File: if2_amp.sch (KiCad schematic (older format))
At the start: 23 parts, among them Q2 BC847BS, U3 MCP6D11

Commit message: Pcb vHA8KDA
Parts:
- added C?: 10n, Capacitor_SMD:C_0805_2012Metric_Pad1.18x1.45mm_HandSolder, symbol Device:C
- added R42, R43: 19k, Resistor_SMD:R_0805_2012Metric_Pad1.20x1.40mm_HandSolder, symbol Device:R
- C31, C32, C36, C37, C38: footprint Capacitor_SMD:C_0805_2012Metric_Pad1.15x1.40mm_HandSolder -> Capacitor_SMD:C_0805_2012Metric_Pad1.18x1.45mm_HandSolder
- R10, R13, R14, R15, R25, R9: footprint Resistor_SMD:R_0805_2012Metric_Pad1.15x1.40mm_HandSolder -> Resistor_SMD:R_0805_2012Metric_Pad1.20x1.40mm_HandSolder
- R12: footprint Resistor_SMD:R_1206_3216Metric_Pad1.42x1.75mm_HandSolder -> Resistor_SMD:R_0805_2012Metric_Pad1.20x1.40mm_HandSolder
- R35, R36, R37, R38, R39, R40, R41: footprint Resistor_SMD:R_1206_3216Metric_Pad1.42x1.75mm_HandSolder -> Resistor_SMD:R_1206_3216Metric_Pad1.30x1.75mm_HandSolder
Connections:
- net +5VA: now also R42.1
- net DC_CM: now also C32.1, R42.2, R43.1
- net GND: now also C32.2, R43.2
- net GNDA: now also C?.2; no longer C32.2
- net at Q2.2 (B1), Q2.5 (B2), R14.2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: now also C?.1; no longer C32.1
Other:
- moved on the sheet: C32
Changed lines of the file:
@@
 F 0 "R9" V 2193 2450 50  0000 C CNN
 F 1 "1.2k" V 2284 2450 50  0000 C CNN
-F 2 "Resistor_SMD:R_0805_2012Metric_Pad1.15x1.40mm_HandSolder" V 2330 2450 50  0001 C CNN
+F 2 "Resistor_SMD:R_0805_2012Metric_Pad1.20x1.40mm_HandSolder" V 2330 2450 50  0001 C CNN
 F 3 "~" H 2400 2450 50  0001 C CNN
 	1    2400 2450
@@
 F 0 "R10" V 2600 3850 50  0000 C CNN
 F 1 "1.2k" V 2500 3850 50  0000 C CNN
-F 2 "Resistor_SMD:R_0805_2012Metric_Pad1.15x1.40mm_HandSolder" V 2330 3850 50  0001 C CNN
+F 2 "Resistor_SMD:R_0805_2012Metric_Pad1.20x1.40mm_HandSolder" V 2330 3850 50  0001 C CNN
 F 3 "~" H 2400 3850 50  0001 C CNN
 	1    2400 3850
@@
 Wire Wire Line
 	3100 3250 3450 3250
-Wire Wire Line
-	2800 3150 2750 3150
 $Comp
 L power:+5VA #PWR0129
@@
 L Device:C C32
 U 1 1 5FEBE468
-P 7350 3500
-F 0 "C32" H 7465 3546 50  0000 L CNN
-F 1 "10n" H 7465 3455 50  0000 L CNN
-F 2 "Capacitor_SMD:C_0805_2012Metric_Pad1.15x1.40mm_HandSolder" H 7388 3350 50  0001 C CNN
-F 3 "~" H 7350 3500 50  0001 C CNN
-	1    7350 3500
+P 3850 4250
+F 0 "C32" H 3965 4296 50  0000 L CNN
+F 1 "10n" H 3965 4205 50  0000 L CNN
+F 2 "Capacitor_SMD:C_0805_2012Metric_Pad1.18x1.45mm_HandSolder" H 3888 4100 50  0001 C CNN
+F 3 "~" H 3850 4250 50  0001 C CNN
+	1    3850 4250
 	1    0    0    -1
 $EndComp
@@
 F 0 "R14" H 8670 3296 50  0000 L CNN
 F 1 "19k" H 8670 3205 50  0000 L CNN
-F 2 "Resistor_SMD:R_0805_2012Metric_Pad1.15x1.40mm_HandSolder" V 8530 3250 50  0001 C CNN
+F 2 "Resistor_SMD:R_0805_2012Metric_Pad1.20x1.40mm_HandSolder" V 8530 3250 50  0001 C CNN
 F 3 "~" H 8600 3250 50  0001 C CNN
 	1    8600 3250
@@
 F 0 "R15" H 8670 3596 50  0000 L CNN
 F 1 "31k" H 8670 3505 50  0000 L CNN
-F 2 "Resistor_SMD:R_0805_2012Metric_Pad1.15x1.40mm_HandSolder" V 8530 3550 50  0001 C CNN
+F 2 "Resistor_SMD:R_0805_2012Metric_Pad1.20x1.40mm_HandSolder" V 8530 3550 50  0001 C CNN
 F 3 "~" H 8600 3550 50  0001 C CNN
 	1    8600 3550
@@
 F 0 "C31" V 7350 2400 50  0000 L CNN
 F 1 "9p" V 7250 2400 50  0000 L CNN
-F 2 "Capacitor_SMD:C_0805_2012Metric_Pad1.15x1.40mm_HandSolder" H 7438 2150 50  0001 C CNN
+F 2 "Capacitor_SMD:C_0805_2012Metric_Pad1.18x1.45mm_HandSolder" H 7438 2150 50  0001 C CNN
 F 3 "~" H 7400 2300 50  0001 C CNN
 	1    7400 2300
@@
 F 0 "R13" V 6250 4300 50  0000 C CNN
 F 1 "2k5" V 6350 4300 50  0000 C CNN
-F 2 "Resistor_SMD:R_0805_2012Metric_Pad1.15x1.40mm_HandSolder" V 6280 4300 50  0001 C CNN
+F 2 "Resistor_SMD:R_0805_2012Metric_Pad1.20x1.40mm_HandSolder" V 6280 4300 50  0001 C CNN
 F 3 "~" H 6350 4300 50  0001 C CNN
 	1    6350 4300
 	0    1    1    0
 $EndComp
-Text HLabel 2800 3150 2    50   Input ~ 0
+Text HLabel 3300 4100 0    50   Input ~ 0
 DC_CM
 Text HLabel 1500 3250 0    50   Input ~ 0
@@
 F 0 "R12" V 1550 3050 50  0000 C CNN
 F 1 "BP" V 1650 3050 50  0000 C CNN
-F 2 "Resistor_SMD:R_1206_3216Metric_Pad1.42x1.75mm_HandSolder" V 1580 3050 50  0001 C CNN
+F 2 "Resistor_SMD:R_0805_2012Metric_Pad1.20x1.40mm_HandSolder" V 1580 3050 50  0001 C CNN
 F 3 "~" H 1650 3050 50  0001 C CNN
 	1    1650 3050
@@
 F 0 "R35" V 1750 3250 50  0000 C CNN
 F 1 "BP" V 1650 3250 50  0000 C CNN
-F 2 "Resistor_SMD:R_1206_3216Metric_Pad1.42x1.75mm_HandSolder" V 1580 3250 50  0001 C CNN
+F 2 "Resistor_SMD:R_1206_3216Metric_Pad1.30x1.75mm_HandSolder" V 1580 3250 50  0001 C CNN
 F 3 "~" H 1650 3250 50  0001 C CNN
 	1    1650 3250
@@
 F 0 "R36" V 6250 3650 50  0000 C CNN
 F 1 "BP" V 6350 3650 50  0000 C CNN
-F 2 "Resistor_SMD:R_1206_3216Metric_Pad1.42x1.75mm_HandSolder" V 6280 3650 50  0001 C CNN
+F 2 "Resistor_SMD:R_1206_3216Metric_Pad1.30x1.75mm_HandSolder" V 6280 3650 50  0001 C CNN
 F 3 "~" H 6350 3650 50  0001 C CNN
 	1    6350 3650
@@
 F 0 "R37" V 6250 3950 50  0000 C CNN
 F 1 "BP" V 6350 3950 50  0000 C CNN
-F 2 "Resistor_SMD:R_1206_3216Metric_Pad1.42x1.75mm_HandSolder" V 6280 3950 50  0001 C CNN
+F 2 "Resistor_SMD:R_1206_3216Metric_Pad1.30x1.75mm_HandSolder" V 6280 3950 50  0001 C CNN
 F 3 "~" H 6350 3950 50  0001 C CNN
 	1    6350 3950
@@
 F 0 "R38" V 8050 2500 50  0000 L CNN
 F 1 "BP" V 8350 2450 50  0000 L CNN
-F 2 "Resistor_SMD:R_1206_3216Metric_Pad1.42x1.75mm_HandSolder" V 8180 2500 50  0001 C CNN
+F 2 "Resistor_SMD:R_1206_3216Metric_Pad1.30x1.75mm_HandSolder" V 8180 2500 50  0001 C CNN
 F 3 "~" H 8250 2500 50  0001 C CNN
 	1    8250 2500
@@
 F 0 "R39" V 8050 2600 50  0000 L CNN
 F 1 "BP" V 8150 2550 50  0000 L CNN
-F 2 "Resistor_SMD:R_1206_3216Metric_Pad1.42x1.75mm_HandSolder" V 8180 2600 50  0001 C CNN
+F 2 "Resistor_SMD:R_1206_3216Metric_Pad1.30x1.75mm_HandSolder" V 8180 2600 50  0001 C CNN
 F 3 "~" H 8250 2600 50  0001 C CNN
 	1    8250 2600
@@
 F 0 "C36" H 9165 3596 50  0000 L CNN
 F 1 "10n" H 9165 3505 50  0000 L CNN
-F 2 "Capacitor_SMD:C_0805_2012Metric_Pad1.15x1.40mm_HandSolder" H 9088 3400 50  0001 C CNN
+F 2 "Capacitor_SMD:C_0805_2012Metric_Pad1.18x1.45mm_HandSolder" H 9088 3400 50  0001 C CNN
 F 3 "~" H 9050 3550 50  0001 C CNN
 	1    9050 3550
@@
 F 0 "C37" H 9565 3596 50  0000 L CNN
 F 1 "100n" H 9565 3505 50  0000 L CNN
-F 2 "Capacitor_SMD:C_0805_2012Metric_Pad1.15x1.40mm_HandSolder" H 9488 3400 50  0001 C CNN
+F 2 "Capacitor_SMD:C_0805_2012Metric_Pad1.18x1.45mm_HandSolder" H 9488 3400 50  0001 C CNN
 F 3 "~" H 9450 3550 50  0001 C CNN
 	1    9450 3550
@@
 F 0 "R25" V 9443 3400 50  0000 C CNN
 F 1 "100" V 9534 3400 50  0000 C CNN
-F 2 "Resistor_SMD:R_0805_2012Metric_Pad1.15x1.40mm_HandSolder" V 9580 3400 50  0001 C CNN
+F 2 "Resistor_SMD:R_0805_2012Metric_Pad1.20x1.40mm_HandSolder" V 9580 3400 50  0001 C CNN
 F 3 "~" H 9650 3400 50  0001 C CNN
 	1    9650 3400
@@
 F 0 "C38" H 10015 3596 50  0000 L CNN
 F 1 "100n" H 10015 3505 50  0000 L CNN
-F 2 "Capacitor_SMD:C_0805_2012Metric_Pad1.15x1.40mm_HandSolder" H 9938 3400 50  0001 C CNN
+F 2 "Capacitor_SMD:C_0805_2012Metric_Pad1.18x1.45mm_HandSolder" H 9938 3400 50  0001 C CNN
 F 3 "~" H 9900 3550 50  0001 C CNN
 	1    9900 3550
@@
 F 0 "R40" V 2850 3050 50  0000 C CNN
 F 1 "BP" V 2950 3050 50  0000 C CNN
-F 2 "Resistor_SMD:R_1206_3216Metric_Pad1.42x1.75mm_HandSolder" V 2880 3050 50  0001 C CNN
+F 2 "Resistor_SMD:R_1206_3216Metric_Pad1.30x1.75mm_HandSolder" V 2880 3050 50  0001 C CNN
 F 3 "~" H 2950 3050 50  0001 C CNN
 	1    2950 3050
@@
 F 0 "R41" V 3050 3250 50  0000 C CNN
 F 1 "BP" V 2950 3250 50  0000 C CNN
-F 2 "Resistor_SMD:R_1206_3216Metric_Pad1.42x1.75mm_HandSolder" V 2880 3250 50  0001 C CNN
+F 2 "Resistor_SMD:R_1206_3216Metric_Pad1.30x1.75mm_HandSolder" V 2880 3250 50  0001 C CNN
 F 3 "~" H 2950 3250 50  0001 C CNN
 	1    2950 3250
@@
 	1    0    0    -1
 $EndComp
+$Comp
+L Device:R R42
+U 1 1 600B0426
+P 3500 3950
+F 0 "R42" H 3570 3996 50  0000 L CNN
+F 1 "19k" H 3570 3905 50  0000 L CNN
+F 2 "Resistor_SMD:R_0805_2012Metric_Pad1.20x1.40mm_HandSolder" V 3430 3950 50  0001 C CNN
+F 3 "~" H 3500 3950 50  0001 C CNN
+	1    3500 3950
+	1    0    0    -1
+$EndComp
+$Comp
+L Device:R R43
+U 1 1 600B1000
+P 3500 4250
+F 0 "R43" H 3570 4296 50  0000 L CNN
+F 1 "19k" H 3570 4205 50  0000 L CNN
+F 2 "Resistor_SMD:R_0805_2012Metric_Pad1.20x1.40mm_HandSolder" V 3430 4250 50  0001 C CNN
+F 3 "~" H 3500 4250 50  0001 C CNN
+	1    3500 4250
+	1    0    0    -1
+$EndComp
+$Comp
+L power:GND #PWR0115
+U 1 1 600B13A7
+P 3500 4400
+F 0 "#PWR0115" H 3500 4150 50  0001 C CNN
+F 1 "GND" H 3500 4250 50  0000 C CNN
+F 2 "" H 3500 4400 50  0001 C CNN
+F 3 "" H 3500 4400 50  0001 C CNN
+	1    3500 4400
+	1    0    0    -1
+$EndComp
+$Comp
+L power:+5VA #PWR0125
+U 1 1 600B17EE
+P 3500 3800
+F 0 "#PWR0125" H 3500 3650 50  0001 C CNN
+F 1 "+5VA" H 3515 3973 50  0000 C CNN
+F 2 "" H 3500 3800 50  0001 C CNN
+F 3 "" H 3500 3800 50  0001 C CNN
+	1    3500 3800
+	1    0    0    -1
+$EndComp
+$Comp
+L power:GND #PWR0143
+U 1 1 600B3B12
+P 3850 4400
+F 0 "#PWR0143" H 3850 4150 50  0001 C CNN
+F 1 "GND" H 3850 4250 50  0000 C CNN
+F 2 "" H 3850 4400 50  0001 C CNN
+F 3 "" H 3850 4400 50  0001 C CNN
+	1    3850 4400
+	1    0    0    -1
+$EndComp
+Wire Wire Line
+	3850 4100 3500 4100
+Connection ~ 3500 4100
+Wire Wire Line
+	3300 4100 3500 4100
+Wire Wire Line
+	3850 3150 3850 4100
+Wire Wire Line
+	2750 3150 3850 3150
+Connection ~ 3850 4100
+$Comp
+L Device:C C?
+U 1 1 600BC4CD
+P 7350 3500
+F 0 "C?" H 7465 3546 50  0000 L CNN
+F 1 "10n" H 7465 3455 50  0000 L CNN
+F 2 "Capacitor_SMD:C_0805_2012Metric_Pad1.18x1.45mm_HandSolder" H 7388 3350 50  0001 C CNN
+F 3 "~" H 7350 3500 50  0001 C CNN
+	1    7350 3500
+	1    0    0    -1
+$EndComp

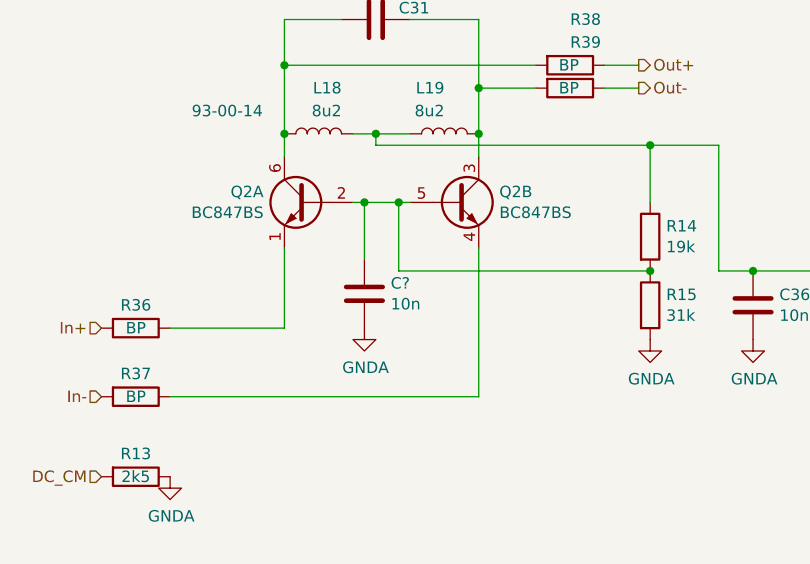
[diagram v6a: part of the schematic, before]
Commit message: Pcb edges and spacer part number
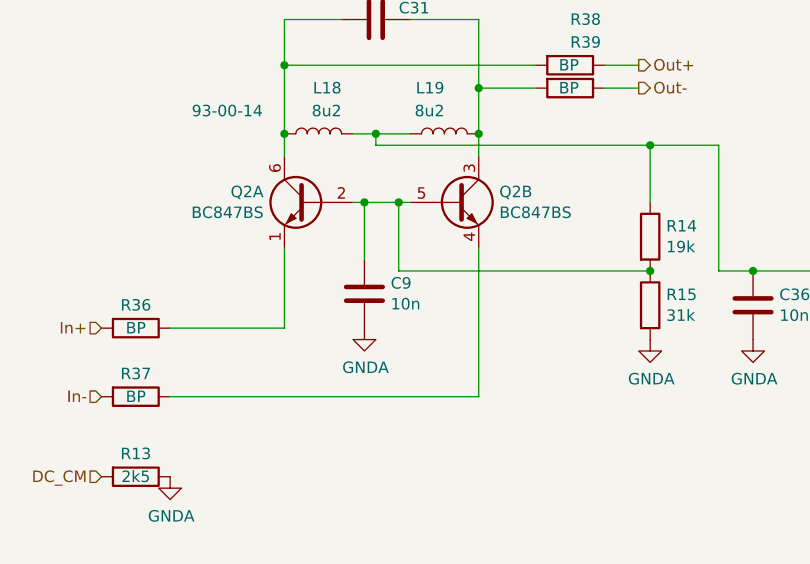
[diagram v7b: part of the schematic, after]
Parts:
- gave numbers to parts that had none: 1
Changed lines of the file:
@@
 Connection ~ 3850 4100
 $Comp
-L Device:C C?
+L Device:C C9
 U 1 1 600BC4CD
 P 7350 3500
-F 0 "C?" H 7465 3546 50  0000 L CNN
+F 0 "C9" H 7465 3546 50  0000 L CNN
 F 1 "10n" H 7465 3455 50  0000 L CNN
 F 2 "Capacitor_SMD:C_0805_2012Metric_Pad1.18x1.45mm_HandSolder" H 7388 3350 50  0001 C CNN

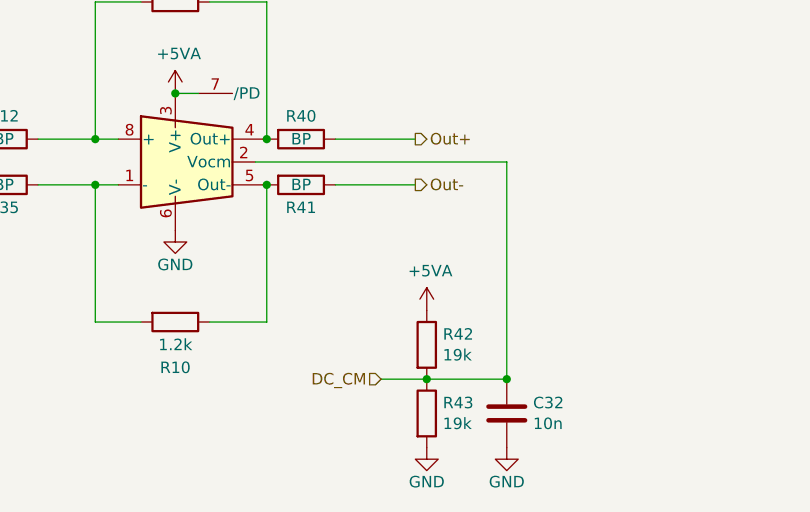
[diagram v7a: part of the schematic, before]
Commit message: diffamp common mode fix
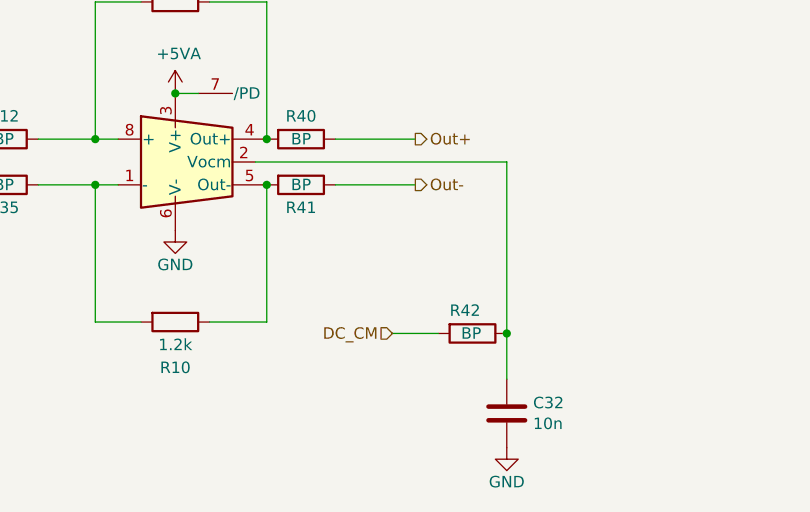
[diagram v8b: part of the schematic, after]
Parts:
- removed R43: 19k, Resistor_SMD:R_0805_2012Metric_Pad1.20x1.40mm_HandSolder, symbol Device:R
- R42: value 19k -> BP
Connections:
- net +5VA: no longer R42.1
- net DC_CM: no longer C32.1, U3.2 (Vocm)
- new net: C32.1, R42.1, U3.2 (Vocm)
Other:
- moved on the sheet: R42
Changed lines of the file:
@@
 	0    1    1    0
 $EndComp
-Text HLabel 3300 4100 0    50   Input ~ 0
+Text HLabel 3350 3900 0    50   Input ~ 0
 DC_CM
 Text HLabel 1500 3250 0    50   Input ~ 0
@@
 L Device:R R42
 U 1 1 600B0426
-P 3500 3950
-F 0 "R42" H 3570 3996 50  0000 L CNN
-F 1 "19k" H 3570 3905 50  0000 L CNN
-F 2 "Resistor_SMD:R_0805_2012Metric_Pad1.20x1.40mm_HandSolder" V 3430 3950 50  0001 C CNN
-F 3 "~" H 3500 3950 50  0001 C CNN
-	1    3500 3950
-	1    0    0    -1
-$EndComp
-$Comp
-L Device:R R43
-U 1 1 600B1000
-P 3500 4250
-F 0 "R43" H 3570 4296 50  0000 L CNN
-F 1 "19k" H 3570 4205 50  0000 L CNN
-F 2 "Resistor_SMD:R_0805_2012Metric_Pad1.20x1.40mm_HandSolder" V 3430 4250 50  0001 C CNN
-F 3 "~" H 3500 4250 50  0001 C CNN
-	1    3500 4250
-	1    0    0    -1
-$EndComp
-$Comp
-L power:GND #PWR0115
-U 1 1 600B13A7
-P 3500 4400
-F 0 "#PWR0115" H 3500 4150 50  0001 C CNN
-F 1 "GND" H 3500 4250 50  0000 C CNN
-F 2 "" H 3500 4400 50  0001 C CNN
-F 3 "" H 3500 4400 50  0001 C CNN
-	1    3500 4400
-	1    0    0    -1
-$EndComp
-$Comp
-L power:+5VA #PWR0125
-U 1 1 600B17EE
-P 3500 3800
-F 0 "#PWR0125" H 3500 3650 50  0001 C CNN
-F 1 "+5VA" H 3515 3973 50  0000 C CNN
-F 2 "" H 3500 3800 50  0001 C CNN
-F 3 "" H 3500 3800 50  0001 C CNN
-	1    3500 3800
-	1    0    0    -1
+P 3700 3900
+F 0 "R42" V 3600 3800 50  0000 L CNN
+F 1 "BP" V 3700 3850 50  0000 L CNN
+F 2 "Resistor_SMD:R_0805_2012Metric_Pad1.20x1.40mm_HandSolder" V 3630 3900 50  0001 C CNN
+F 3 "~" H 3700 3900 50  0001 C CNN
+	1    3700 3900
+	0    1    1    0
 $EndComp
 $Comp
@@
 $EndComp
 Wire Wire Line
-	3850 4100 3500 4100
-Connection ~ 3500 4100
-Wire Wire Line
-	3300 4100 3500 4100
-Wire Wire Line
-	3850 3150 3850 4100
+	3350 3900 3550 3900
+Wire Wire Line
+	3850 3150 3850 3900
 Wire Wire Line
 	2750 3150 3850 3150
-Connection ~ 3850 4100
 $Comp
 L Device:C C9
@@
 	1    0    0    -1
 $EndComp
+Connection ~ 3850 3900
+Wire Wire Line
+	3850 3900 3850 4100
 $EndSCHEMATC
